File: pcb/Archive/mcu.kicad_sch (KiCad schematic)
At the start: 21 parts, among them J3 USB_C_USB2.0_16P, SW1 EVQ-Q2B02W, SW2 EVQ-Q2B02W, U1 ESP32-S3-WROOM-1-N8R2, U4 USBLC6-2P6

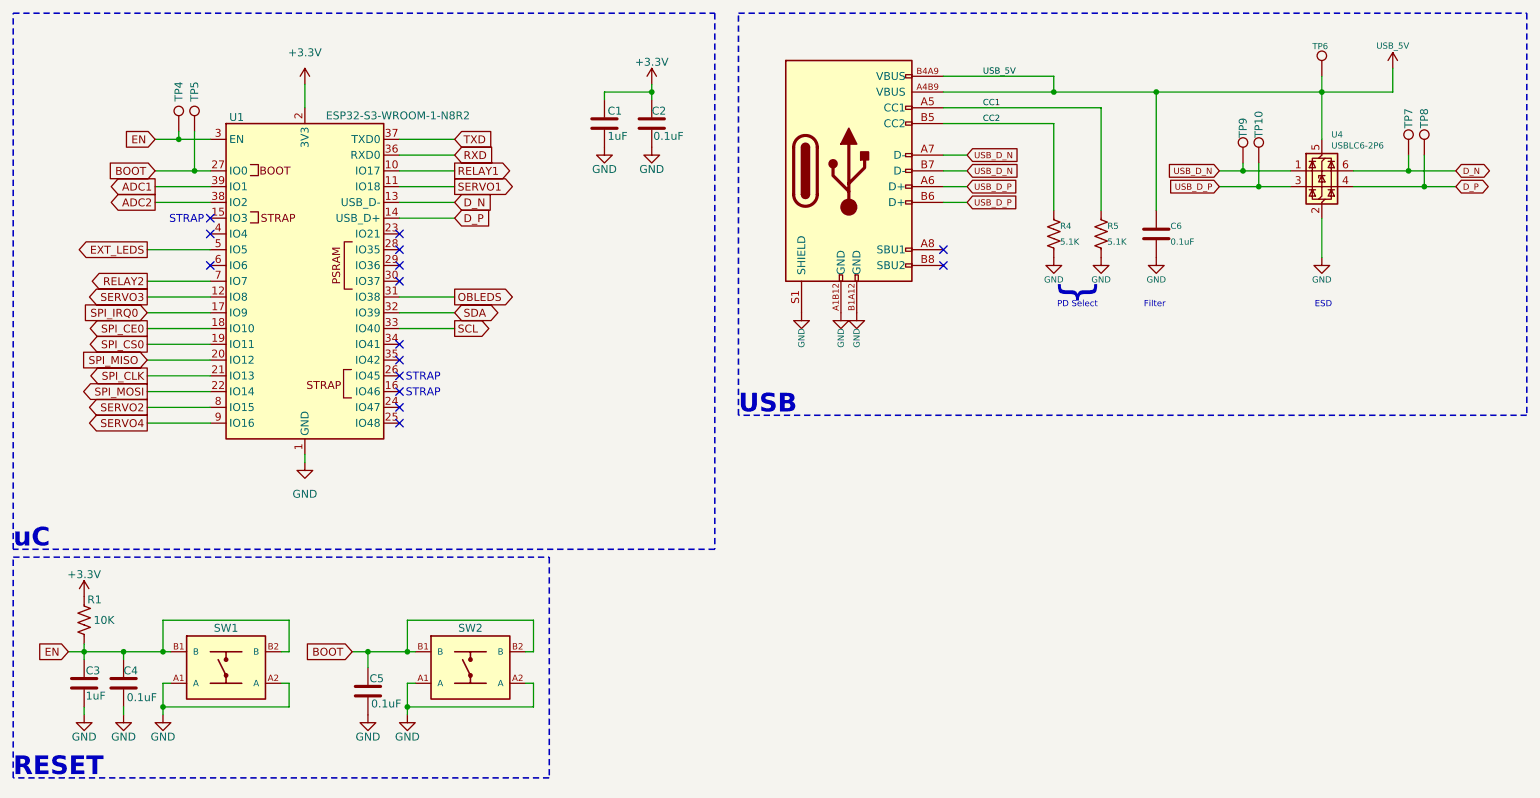
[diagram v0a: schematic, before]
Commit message: Added interfaces and fully routed PCB
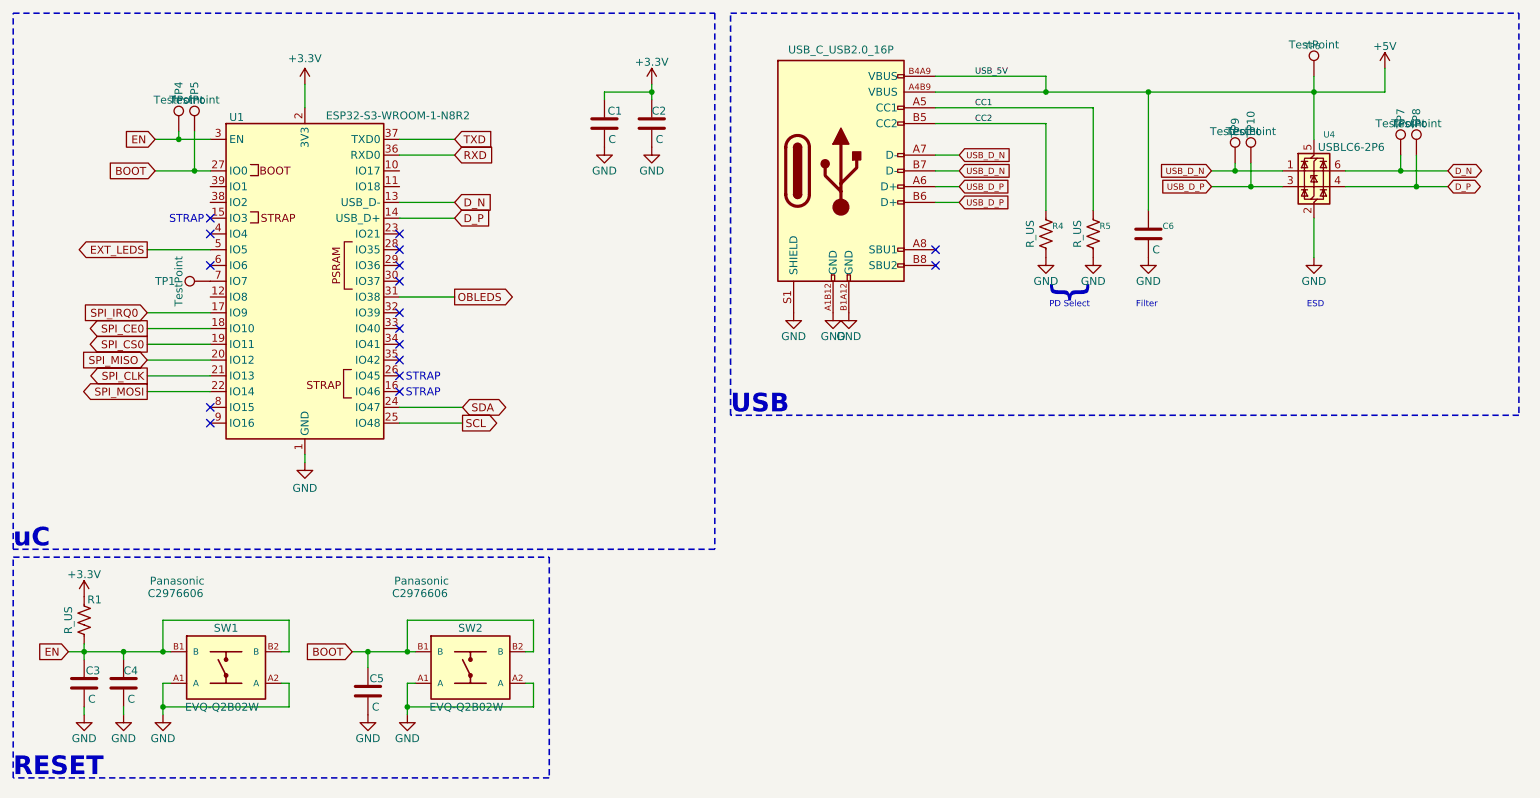
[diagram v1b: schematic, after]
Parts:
- added TP1: TestPoint, symbol Connector:TestPoint
- C1: value 1uF -> C; footprint Capacitor_SMD:C_0603_1608Metric -> (none); Digikey 1276-1019-2-ND -> (none); LCSC C6119849 -> (none); MN HRE -> (none); MPN CGA0603X5R105K160JT -> (none); Mouser 187-CL10B105KO8NNNC -> (none)
- C2: value 0.1uF -> C; footprint Capacitor_SMD:C_0603_1608Metric -> (none); LCSC C15849 -> (none); MN Samsung -> (none); MPN CL10A105KB8NNNC -> (none)
- C3: value 1uF -> C; footprint Capacitor_SMD:C_0603_1608Metric -> (none); Dielectric X5R -> (none); Digikey 1276-1019-2-ND -> (none); LCSC C6119849 -> (none); MN HRE -> (none); MPN CGA0603X5R105K160JT -> (none); Mouser 187-CL10B105KO8NNNC -> (none); Tolerance 10% -> (none); WVDC 16V -> (none)
- C4, C5, C6: value 0.1uF -> C; footprint Capacitor_SMD:C_0603_1608Metric -> (none); Digikey 1276-1005-2-ND -> (none); LCSC C66501 -> (none); MN Samsung -> (none); MPN CL10B104KO8NNNC -> (none); Mouser 187-CL10B104KO8NNNC -> (none)
- R1: value 10K -> R_US; footprint Resistor_SMD:R_0603_1608Metric -> (none); Digikey CR0603-JW-103ELFTR-ND -> (none); LCSC C2930027 -> (none); MN FOJAN -> (none); MPN FRC0603J103TS -> (none); Mouser 652-CR0603-JW-103ELF -> (none)
- R4, R5: value 5.1K -> R_US; footprint Resistor_SMD:R_0603_1608Metric -> (none); Digikey 118-CR0603-JW-512ELFTR-ND -> (none); LCSC C2907114 -> (none); MN FOJAN -> (none); MPN FRC0603J512 TS -> (none); Mouser 652-CR0603JW-512ELF -> (none)
- SW1, SW2: Digikey P12931STR-ND -> (none); LCSC C2976606 -> (none); LCSC_PN (none) -> C2976606; MF (none) -> Panasonic; MN Panasonic -> (none); Mouser 667-EVQ-Q2B02W -> (none)
- TP10, TP4, TP5, TP6, TP7, TP8, TP9: value ~ -> TestPoint; footprint CRGM Mechanical:TestPoint_Pad_D1.0mm -> (none); now in the parts list
- U4: Digikey 497-5026-2-ND -> (none); LCSC C2827693 -> (none); MN TECH PUBLIC -> (none); MPN USBLC6-2P6 -> (none); Mouser 511-USBLC6-2P6 -> (none)
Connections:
- net SCL: now also U1.25 (IO48); no longer U1.33 (IO40)
- net SDA: now also U1.24 (IO47); no longer U1.32 (IO39)
- net ADC1: no longer names the net of U1.39 (IO1)
- net ADC2: no longer names the net of U1.38 (IO2)
- net RELAY1: no longer names the net of U1.10 (IO17)
- net RELAY2: no longer names the net of U1.7 (IO7)
- net RELAY2: now also TP1.1
- net SERVO1: no longer names the net of U1.11 (IO18)
- net SERVO2: no longer names the net of U1.8 (IO15)
- net SERVO3: no longer names the net of U1.12 (IO8)
- net SERVO4: no longer names the net of U1.9 (IO16)
- net USB_5V renamed +5V
- no-connect marks 15 -> 17
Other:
- moved on the sheet: C6, R4, R5, TP10, TP6, TP7, TP8, TP9, U4
